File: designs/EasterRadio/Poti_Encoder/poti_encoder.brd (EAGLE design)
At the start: 50 x 33 mm, 12 parts

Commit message: final changes ready for purchase
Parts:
- moved ENC 0.50 mm to (40.3, 23.5)
- moved POTI 0.50 mm to (6.53, 16.5)

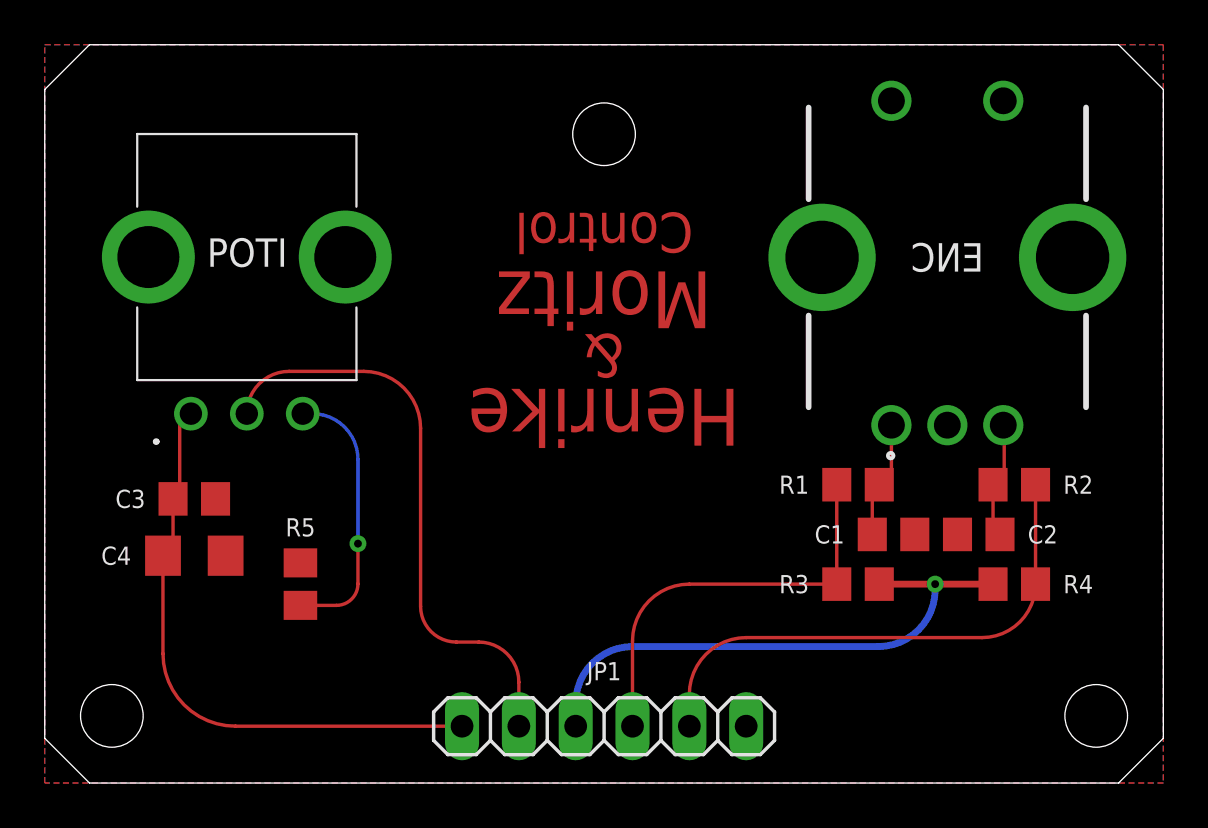
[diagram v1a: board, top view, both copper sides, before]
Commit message: changed poti and encoder pcb to correct schematic and brd + mainboard change for push btn on rotary encoder
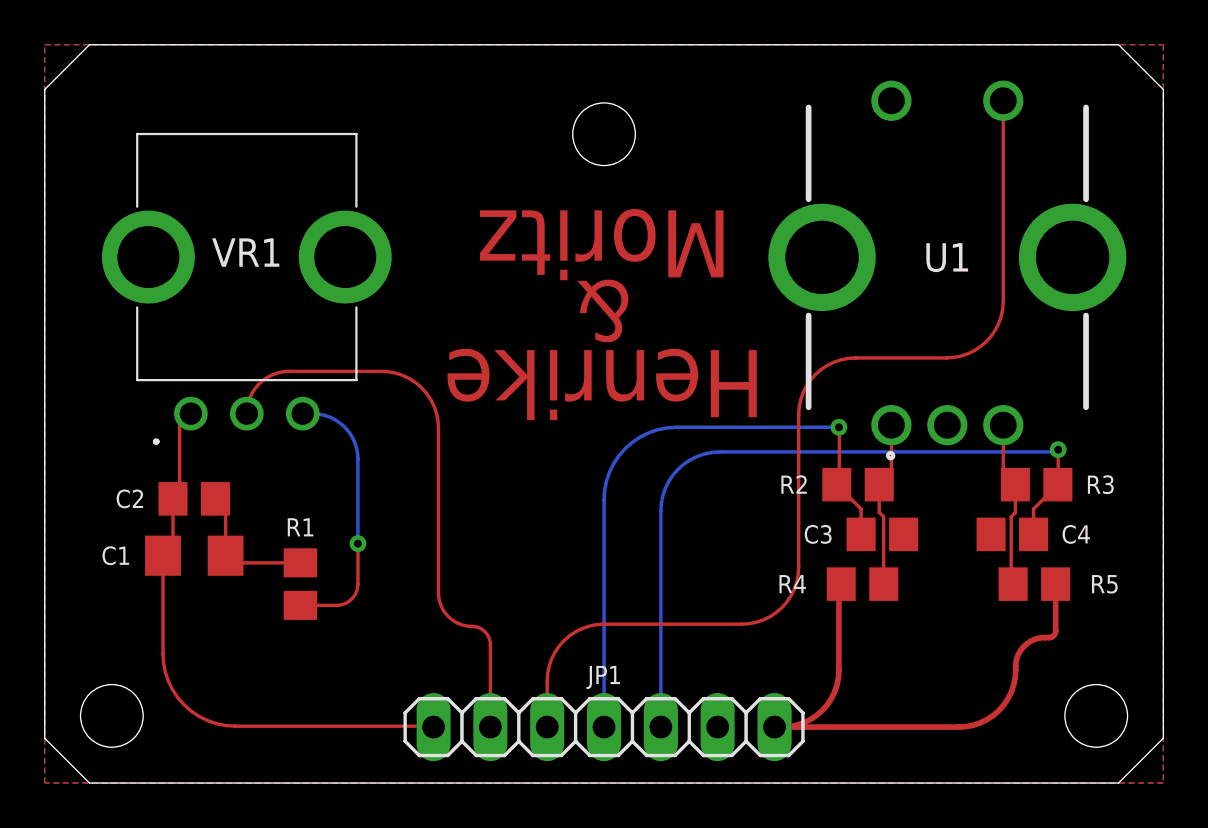
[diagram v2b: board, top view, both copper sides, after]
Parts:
- C1: value (none) -> 47uF; device CommonParts:C0805 -> CommonParts:C1206
- C2: value (none) -> 1uF
- C3: value 1uF -> (none)
- C4: value 47uF -> (none); device CommonParts:C1206 -> CommonParts:C0805
- JP1: device pinhead:1X06 -> pinhead:1X07
- R1: value 10kohm -> 100ohm
- R5: value 100ohm -> 10kohm
- moved C4 36.6 mm to (43.2, 11.1), turned to 180 degrees
- moved C2 35.1 mm to (6.68, 12.7), turned to 0 degrees
- moved R5 32.8 mm to (44.2, 8.89), turned to 180 degrees
- moved C1 31.3 mm to (6.68, 10.2), turned to 0 degrees
- moved C3 30.8 mm to (37.4, 11.1), turned to 180 degrees
- moved R1 25.3 mm to (11.4, 8.89), turned to 270 degrees
- moved R3 9.14 mm to (44.3, 13.3), turned to 180 degrees
- moved R2 6.98 mm to (36.4, 13.3), turned to 0 degrees
- moved R4 6.78 mm to (36.6, 8.89), turned to 180 degrees
- renumbered ENC to U1, POTI to VR1
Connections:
- new net PUSH: JP1.3, U1.5
- net 3.3V: now also JP1.7, R4.2, R5.1; no longer JP1.3, R3.2, R4.1
- net ENC_A: now also C3.2, R2.1; no longer R1.1, R3.1
- net ENC_B: now also C4.1, R3.1; no longer R2.1, R4.2
- net GNDA: now also C1.2, C3.1, R1.1, U1.4; no longer C1.1, C3.2, R5.1
- net N$1: now also R2.2, R4.1; no longer C1.2, R1.2
- net N$2: now also R3.2, R5.2; no longer C2.1, R2.2
- net N$4: now also R1.2; no longer R5.2
- net TUNE1: now also C1.1, C2.1; no longer C3.1, C4.1
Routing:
- net PUSH: track 0.00 -> 42.4 mm
- net ENC_B: track 23.4 -> 33.3 mm, vias 0 -> 1
- net ENC_A: track 18.4 -> 27.4 mm, vias 0 -> 1
- net GNDA: track 0.00 -> 6.68 mm
- net N$1: track 5.24 -> 8.62 mm
- net N$2: track 5.24 -> 7.54 mm
- net TUNE1: track 26.0 -> 24.7 mm
- net TUNE2: track 25.3 -> 24.7 mm
- net 3.3V: track 24.5 -> 24.4 mm, vias 1 -> 0
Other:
- board text removed: "Control"

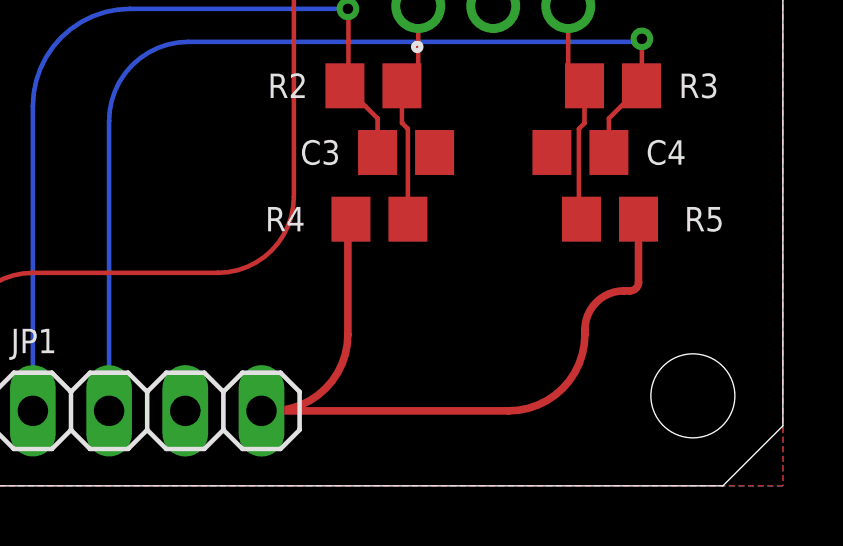
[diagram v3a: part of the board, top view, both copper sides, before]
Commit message: added new design of radio parts added 3.3V mark
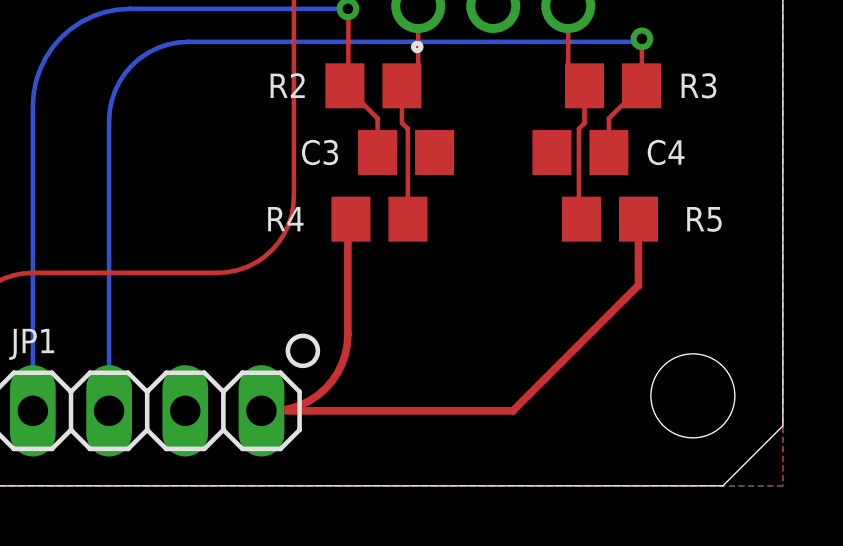
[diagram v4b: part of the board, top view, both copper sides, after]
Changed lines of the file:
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@@
 <drawing>
 <settings>
-<setting alwaysvectorfont="yes"/>
+<setting alwaysvectorfont="no"/>
 <setting verticaltext="up"/>
 </settings>
@@
 </layers>
 <board>
-<fusionsync huburn="a.cGVyc29uYWw6dWUyYTNmMDU1" projecturn="a.cGVyc29uYWw6dWUyYTNmMDU1IzIwMTgxMjEwMTY0OTQ5MjI2" f3durn="urn:adsk.wipprod:dm.lineage:y21_RZBvSAORnGwvAKpn-g" pcbguid="8b1540f9-6f3a-45d8-8af4-96b17c034e04" lastpulledtime="" lastsyncedchangeguid="" latestrevisionid="93666ca1-369e-4fa8-b184-ce4617967a8b" lastsyncedrevisionid="93666ca1-369e-4fa8-b184-ce4617967a8b" lastboardhashguid="e622a0e1-90d9-f4ce-1641-76ed55730201" lastpushedtime="2021-02-03T18:11:52Z" linktopcb3d="true"/>
+<fusionsync huburn="a.cGVyc29uYWw6dWUyYTNmMDU1" projecturn="a.cGVyc29uYWw6dWUyYTNmMDU1IzIwMTgxMjEwMTY0OTQ5MjI2" f3durn="urn:adsk.wipprod:dm.lineage:y21_RZBvSAORnGwvAKpn-g" pcbguid="" lastpulledtime="" lastsyncedchangeguid="" latestrevisionid="480782c5-31a4-4f71-bf40-244998a76887" lastsyncedrevisionid="480782c5-31a4-4f71-bf40-244998a76887" lastboardhashguid="95b43093-735d-034b-58b8-7eedfa376b11" lastpushedtime="2021-03-15T17:48:25Z" linktopcb3d="true"/>
 <plain>
 <hole x="25" y="29" drill="2.8"/>
@@
 <hole x="3" y="3" drill="2.8"/>
 <circle x="3" y="3" radius="1.4142125" width="2.54" layer="41"/>
+<circle x="34" y="4.5" radius="0.5" width="0.1524" layer="25"/>
+<circle x="47" y="3" radius="1.4142125" width="2.54" layer="42"/>
+<circle x="3" y="3" radius="1.4142125" width="2.54" layer="42"/>
+<circle x="25" y="29" radius="1.4142125" width="2.54" layer="42"/>
 </plain>
 <attributes>
@@
 <wire x1="32.96" y1="2.5" x2="35.5" y2="5.04" width="0.254" layer="1" curve="90"/>
 <wire x1="35.5" y1="5.04" x2="35.5" y2="8.7875" width="0.254" layer="1"/>
-<wire x1="32.62" y1="2.5" x2="40.86" y2="2.5" width="0.254" layer="1"/>
-<wire x1="40.86" y1="2.5" x2="43.4" y2="5.04" width="0.254" layer="1" curve="90"/>
-<wire x1="43.4" y1="5.04" x2="43.4" y2="5.2" width="0.254" layer="1"/>
-<wire x1="43.4" y1="5.2" x2="44.7" y2="6.5" width="0.254" layer="1" curve="-90"/>
-<wire x1="44.7" y1="6.5" x2="44.9" y2="6.5" width="0.254" layer="1"/>
-<wire x1="44.9" y1="6.5" x2="45.1875" y2="6.7875" width="0.254" layer="1" curve="90"/>
-<wire x1="45.1875" y1="6.7875" x2="45.1875" y2="8.89" width="0.254" layer="1"/>
+<wire x1="32.62" y1="2.5" x2="41" y2="2.5" width="0.254" layer="1"/>
+<wire x1="41" y1="2.5" x2="45.1875" y2="6.6875" width="0.254" layer="1"/>
+<wire x1="45.1875" y1="6.6875" x2="45.1875" y2="8.89" width="0.254" layer="1"/>
 </signal>
 <signal name="GNDA">

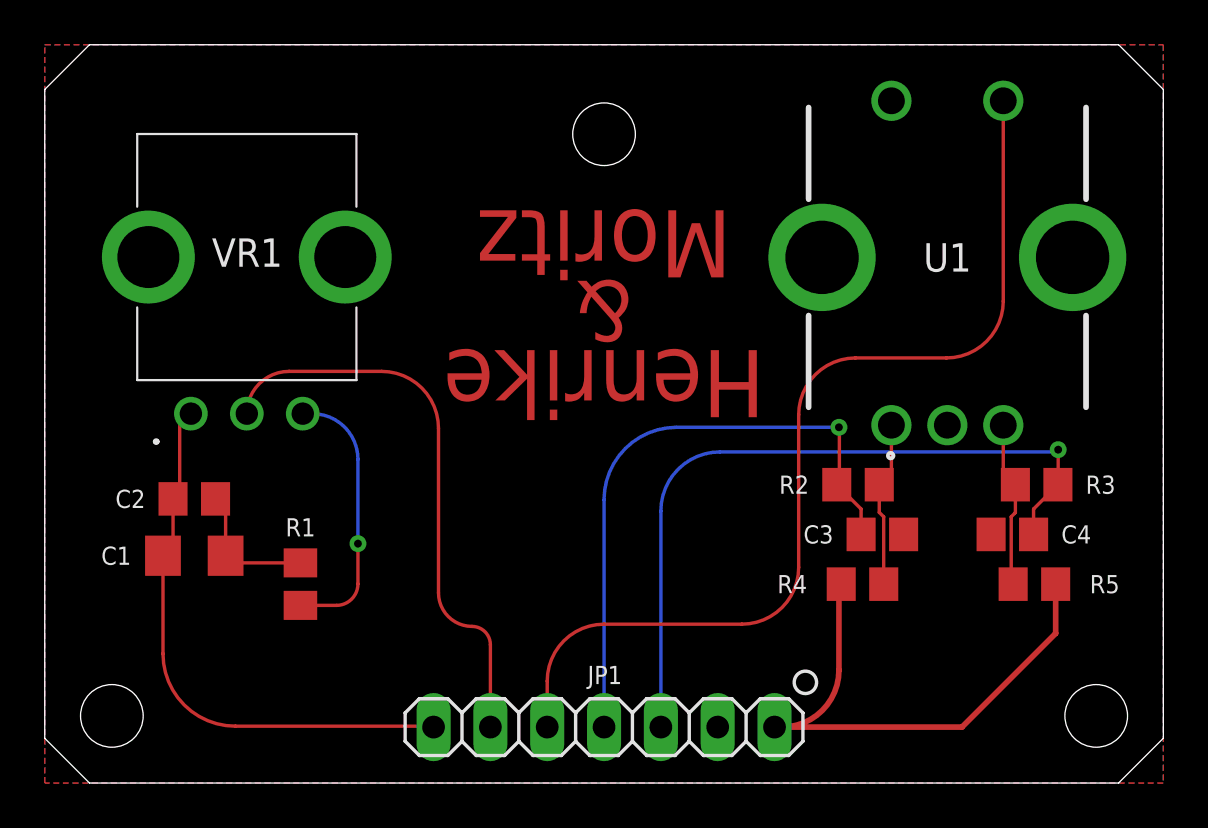
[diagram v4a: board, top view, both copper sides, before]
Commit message: Fixed encoder issue: Terminal C connected to 3.3V instead of GND which is in contrast to the datasheet circuit diagram but is working.
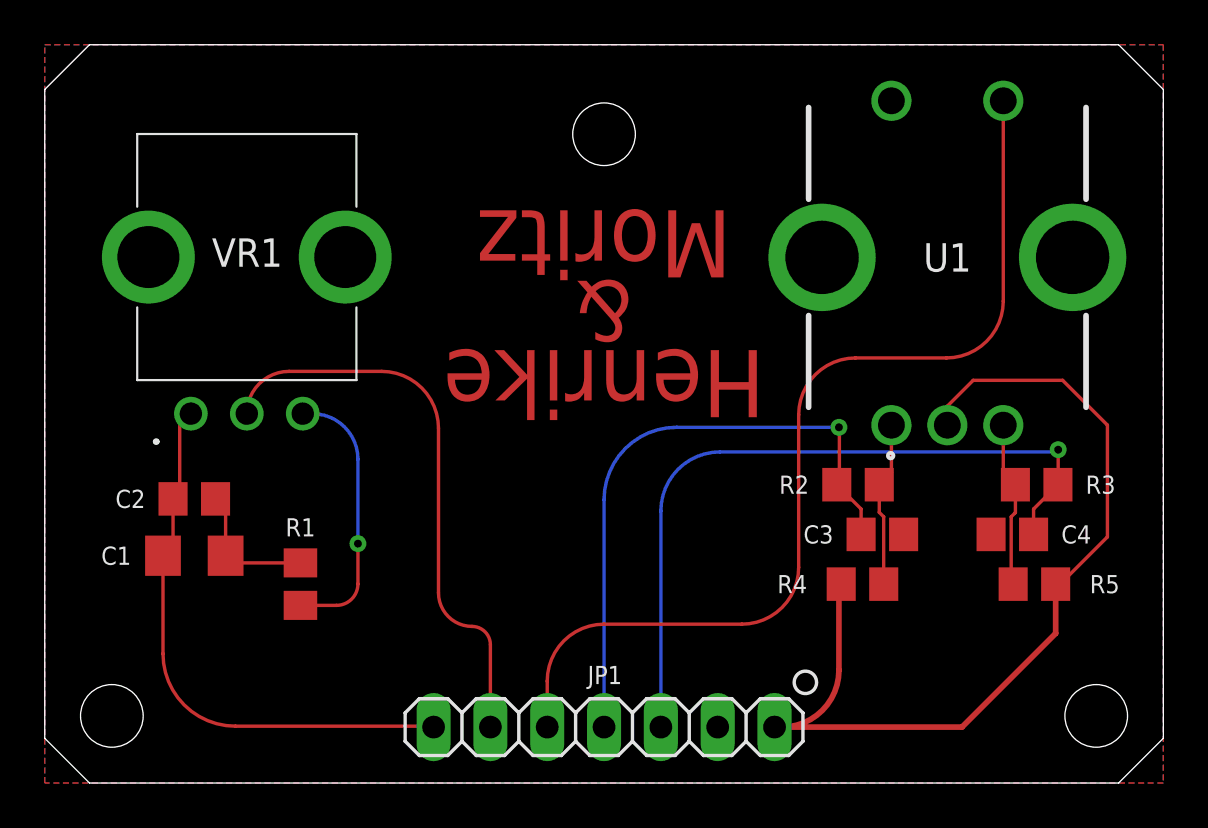
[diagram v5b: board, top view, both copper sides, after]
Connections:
- net 3.3V: now also U1.3
- net GNDA: no longer U1.3
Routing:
- net 3.3V: track 24.3 -> 41.8 mm
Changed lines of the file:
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@@
 </layers>
 <board>
-<fusionsync huburn="a.cGVyc29uYWw6dWUyYTNmMDU1" projecturn="a.cGVyc29uYWw6dWUyYTNmMDU1IzIwMTgxMjEwMTY0OTQ5MjI2" f3durn="urn:adsk.wipprod:dm.lineage:y21_RZBvSAORnGwvAKpn-g" pcbguid="" lastpulledtime="" lastsyncedchangeguid="" latestrevisionid="480782c5-31a4-4f71-bf40-244998a76887" lastsyncedrevisionid="480782c5-31a4-4f71-bf40-244998a76887" lastboardhashguid="95b43093-735d-034b-58b8-7eedfa376b11" lastpushedtime="2021-03-15T17:48:25Z" linktopcb3d="true"/>
+<fusionsync huburn="a.cGVyc29uYWw6dWUyYTNmMDU1" projecturn="a.cGVyc29uYWw6dWUyYTNmMDU1IzIwMTgxMjEwMTY0OTQ5MjI2" f3durn="urn:adsk.wipprod:dm.lineage:y21_RZBvSAORnGwvAKpn-g" pcbguid="" lastpulledtime="" lastsyncedchangeguid="" latestrevisionid="480782c5-31a4-4f71-bf40-244998a76887" lastsyncedrevisionid="480782c5-31a4-4f71-bf40-244998a76887" lastboardhashguid="95b43093-735d-034b-58b8-7eedfa376b11" lastpushedtime="2021-03-15T17:48:25Z" linktopcb3d="false"/>
 <plain>
 <hole x="25" y="29" drill="2.8"/>
@@
 <wire x1="41" y1="2.5" x2="45.1875" y2="6.6875" width="0.254" layer="1"/>
 <wire x1="45.1875" y1="6.6875" x2="45.1875" y2="8.89" width="0.254" layer="1"/>
+<contactref element="U1" pad="3"/>
+<wire x1="40.345" y1="15.995" x2="40.345" y2="16.845" width="0.1524" layer="1"/>
+<wire x1="40.345" y1="16.845" x2="41.5" y2="18" width="0.1524" layer="1"/>
+<wire x1="41.5" y1="18" x2="45.49999375" y2="18" width="0.1524" layer="1"/>
+<wire x1="47.5" y1="16" x2="45.49999375" y2="18" width="0.1524" layer="1"/>
+<wire x1="47.5" y1="16" x2="47.5" y2="11" width="0.1524" layer="1"/>
+<wire x1="45.39" y1="8.89" x2="45.1875" y2="8.89" width="0.1524" layer="1"/>
+<wire x1="47.5" y1="11" x2="45.39" y2="8.89" width="0.1524" layer="1"/>
 </signal>
 <signal name="GNDA">
 <contactref element="C4" pad="2"/>
 <contactref element="C3" pad="1"/>
-<contactref element="U1" pad="3"/>
 <contactref element="C1" pad="2"/>
 <contactref element="C2" pad="2"/>
@@
 <wire x1="8.085" y1="10.16" x2="8.405" y2="9.84" width="0.1524" layer="1"/>
 <wire x1="8.405" y1="9.84" x2="11.43" y2="9.84" width="0.1524" layer="1"/>
-<wire x1="11.77" y1="9.5" x2="11.43" y2="9.84" width="0.1524" layer="1"/>
+<wire x1="11.43" y1="9.84" x2="11.77" y2="9.5" width="0.1524" layer="1"/>
 </signal>
 <signal name="ENC_A">

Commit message: added final revisions to amplifier power radio ic and control pcbs
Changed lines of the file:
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@@
 </layers>
 <board>
-<fusionsync huburn="a.cGVyc29uYWw6dWUyYTNmMDU1" projecturn="a.cGVyc29uYWw6dWUyYTNmMDU1IzIwMTgxMjEwMTY0OTQ5MjI2" f3durn="urn:adsk.wipprod:dm.lineage:y21_RZBvSAORnGwvAKpn-g" pcbguid="" lastpulledtime="" lastsyncedchangeguid="" latestrevisionid="480782c5-31a4-4f71-bf40-244998a76887" lastsyncedrevisionid="480782c5-31a4-4f71-bf40-244998a76887" lastboardhashguid="95b43093-735d-034b-58b8-7eedfa376b11" lastpushedtime="2021-03-15T17:48:25Z" linktopcb3d="false"/>
+<fusionsync huburn="a.cGVyc29uYWw6dWUyYTNmMDU1" projecturn="a.cGVyc29uYWw6dWUyYTNmMDU1IzIwMTgxMjEwMTY0OTQ5MjI2" f3durn="urn:adsk.wipprod:dm.lineage:y21_RZBvSAORnGwvAKpn-g" pcbguid="" lastpulledtime="" lastsyncedchangeguid="" latestrevisionid="480782c5-31a4-4f71-bf40-244998a76887" lastsyncedrevisionid="480782c5-31a4-4f71-bf40-244998a76887" lastboardhashguid="95b43093-735d-034b-58b8-7eedfa376b11" lastpushedtime="2021-03-15T17:48:25Z" linktopcb3d="true"/>
 <plain>
 <hole x="25" y="29" drill="2.8"/>
@@
 <contactref element="R2" pad="2"/>
 <contactref element="U1" pad="1"/>
-<wire x1="36.99" y1="13.0225" x2="37.3025" y2="13.335" width="0.1524" layer="1" curve="-90"/>
 <wire x1="37.845" y1="13.8775" x2="37.3025" y2="13.335" width="0.1524" layer="1" curve="-90"/>
 <contactref element="R4" pad="1"/>
@@
 <contactref element="U1" pad="2"/>
 <contactref element="R3" pad="2"/>
-<wire x1="42.845" y1="15.995" x2="42.8875" y2="15.9525" width="0.1524" layer="1"/>
 <contactref element="R5" pad="2"/>
 <wire x1="43.3875" y1="13.335" x2="43.3875" y2="13.3" width="0.1524" layer="1"/>
@@
 <wire x1="8.085" y1="10.16" x2="8.405" y2="9.84" width="0.1524" layer="1"/>
 <wire x1="8.405" y1="9.84" x2="11.43" y2="9.84" width="0.1524" layer="1"/>
-<wire x1="11.43" y1="9.84" x2="11.77" y2="9.5" width="0.1524" layer="1"/>
 </signal>
 <signal name="ENC_A">
@@
 <contactref element="C4" pad="1"/>
 <contactref element="JP1" pad="5"/>
-<wire x1="45.5" y1="13.1225" x2="45.36125" y2="13.26125" width="0.1524" layer="1"/>
 <wire x1="45.36125" y1="13.26125" x2="45.2875" y2="13.335" width="0.1524" layer="1"/>
 <wire x1="45.2875" y1="13.335" x2="44.2" y2="12.2475" width="0.1524" layer="1"/>
 <wire x1="44.2" y1="12.2475" x2="44.2" y2="11.1125" width="0.1524" layer="1"/>
-<wire x1="44.2125" y1="11.1" x2="44.2" y2="11.1125" width="0.1524" layer="1" curve="-90"/>
 <wire x1="27.54" y1="2.5" x2="27.54" y2="12.16" width="0.1524" layer="16"/>
 <wire x1="27.54" y1="12.16" x2="30.18" y2="14.8" width="0.1524" layer="16" curve="-90"/>
@@
 <mfgpreviewcolor name="substratecolor" color="0xFF786E46"/>
 </mfgpreviewcolors>
-<errors>
-</errors>
 </board>
 </drawing>
